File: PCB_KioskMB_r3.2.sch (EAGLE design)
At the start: 341 parts, among them IC1 ISL60002DIH325Z-TK, IC18 FT232RL, IC19 MCP6022-I/ST, IC2 SN65HVD12D, IC20 LTC1771EMS8, IC21 LTC1771EMS8, IC3 PIC24FJ256GA110-I/PT, IC4 PIC10F200T-I/OT, IC5 LM75ADP, IC6 24LC32A-I/MS, IC7 PCF2123TS/1-T, IC8 M25P16-VMN6P, IC9 LM3405AXMK/NOPB, J1 DF11-10DP-2DSA(01), J10 CCM03-3504LFT-NR, J13 3-641215-3, J14 3-641215-2, J15 3-641215-4, J16 3-641215-4, J40 DNP, J43 3-641215-4, J44 3-641215-4, J45 3-641215-4, J46 3-641215-5, J47 DF11-10DP-2DSA(01), J48 3-641215-2, J49 3-641215-2, J5 3-641215-2, J6 3-641215-2, J7 SS-6566-NF, J8 TSW-108-07-G-D, J9 SS-6566-NF, Q1 SSM6P49NU,LFPZ, Q14 TSM9938HEUK+T, Q15 SI4564DY, Q16 CSD87331Q3D, Q17 TSM9938HEUK+T, Q18 SI4564DY, Q19 CSD87331Q3D, Q2 FDC6330L, Q20 IPD30N06S2L-23, Q21 IPD30N06S2L-23, Q22 FDN352AP, Q23 FDN352AP, Q24 BSS138, Q3 SR3.3.TCT, Q4 7B-28.63636MAAJ-T, Q5 FDC6324L, Q6 CM519 32.768KDZF-UT, Q7 SSM6P49NU,LFPZ, Q8 IPD30N06S2L-23, Q9 IPD30N06S2L-23, U1 LTC1955, U2 HRXL-MAXSONAR-WRC-MB7387, U3 ADS1015, U6 TPS43061, U7 TPS43061, U8 TPA3111D1PWP, U9 OPA322SAIDBVT, X1 FH12-10S-0.5SH

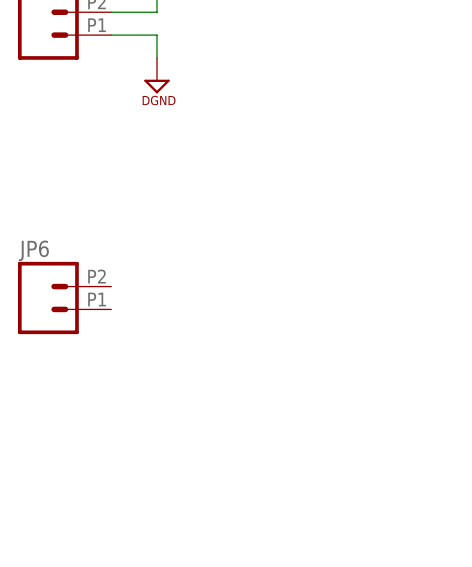
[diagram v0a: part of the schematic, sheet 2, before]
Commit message: almost there again. fixed FPC connector to be 1.00mm pitch.
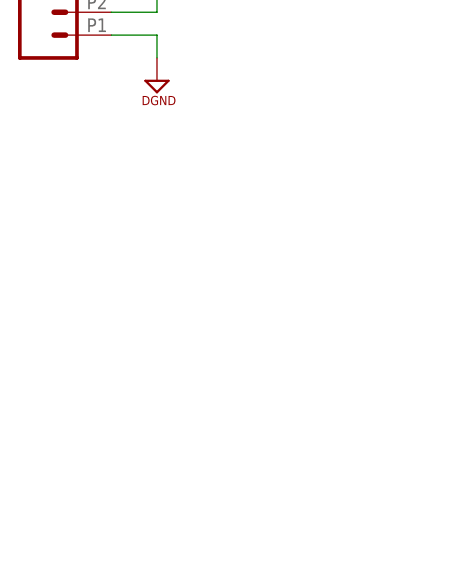
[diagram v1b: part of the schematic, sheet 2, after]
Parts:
- removed JP6: (no value), ChipTestJig:M022.54MM_SCREWTERM
- X1: value FH12-10S-0.5SH -> FH12-10S-0.5S1.00MM; device con-hirose:FH12-10S-0.5SH -> con-hirose:FH12-10S-0.5S1.00MM
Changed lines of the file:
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@@
 <?xml version="1.0" encoding="utf-8"?>
 <!DOCTYPE eagle SYSTEM "eagle.dtd">
-<eagle version="8.2.0">
+<eagle version="8.1.1">
 <drawing>
 <settings>
@@
 <part name="H5" library="SparkFun-Hardware" deviceset="STANDOFF_ELECTRICAL" device=""/>
 <part name="H6" library="SparkFun-Hardware" deviceset="STANDOFF_ELECTRICAL" device=""/>
-<part name="X1" library="con-hirose" deviceset="FH12-10S-0.5S" device="H"/>
+<part name="X1" library="con-hirose" deviceset="FH12-10S-0.5S" device="1.00MM" value="FH12-10S-0.5S1.00MM"/>
 <part name="U$90" library="SUPPLY" deviceset="DGND" device=""/>
 <part name="Q8" library="InfineonTech-AON" deviceset="IPD30N06S2L-23" device=""/>
@@
 <part name="JP4" library="ChipTestJig" deviceset="M02" device="2.54MM_SCREWTERM"/>
 <part name="JP5" library="ChipTestJig" deviceset="M02" device="2.54MM_SCREWTERM"/>
-<part name="JP6" library="ChipTestJig" deviceset="M02" device="2.54MM_SCREWTERM"/>
 <part name="CN1" library="adafruit" deviceset="DCBARREL" device="PTH"/>
 <part name="U$109" library="SUPPLY" deviceset="+SMB" device=""/>
@@
 <instance part="JP4" gate="G$1" x="53.34" y="213.36"/>
 <instance part="JP5" gate="G$1" x="53.34" y="195.58"/>
-<instance part="JP6" gate="G$1" x="53.34" y="165.1"/>
 <instance part="CN1" gate="G$1" x="55.88" y="259.08"/>
 <instance part="U$109" gate="G$1" x="66.04" y="203.2"/>
